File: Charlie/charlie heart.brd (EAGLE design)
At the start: 46.7 x 57.7 mm, 32 parts, among them Q1 BSS84, U1 ATTINY841

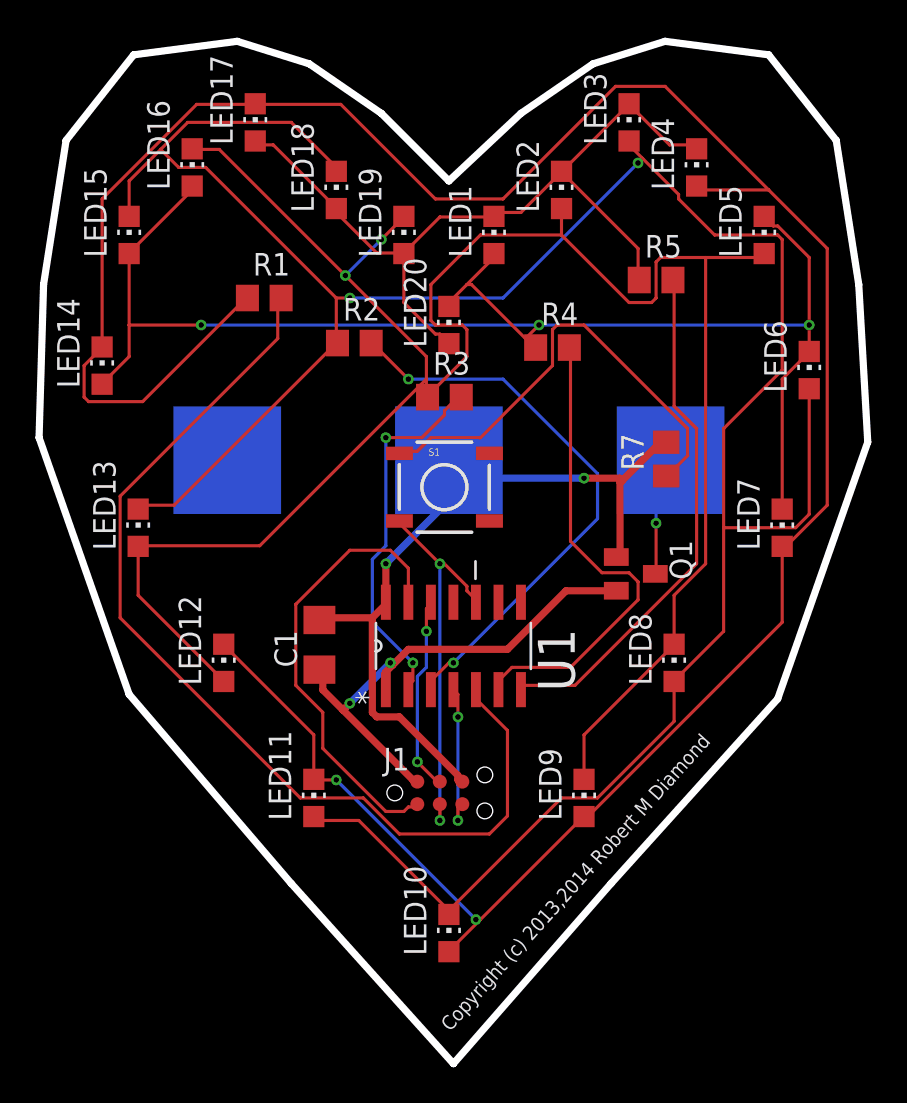
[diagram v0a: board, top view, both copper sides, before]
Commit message: add jumpers for serial and beat sensor
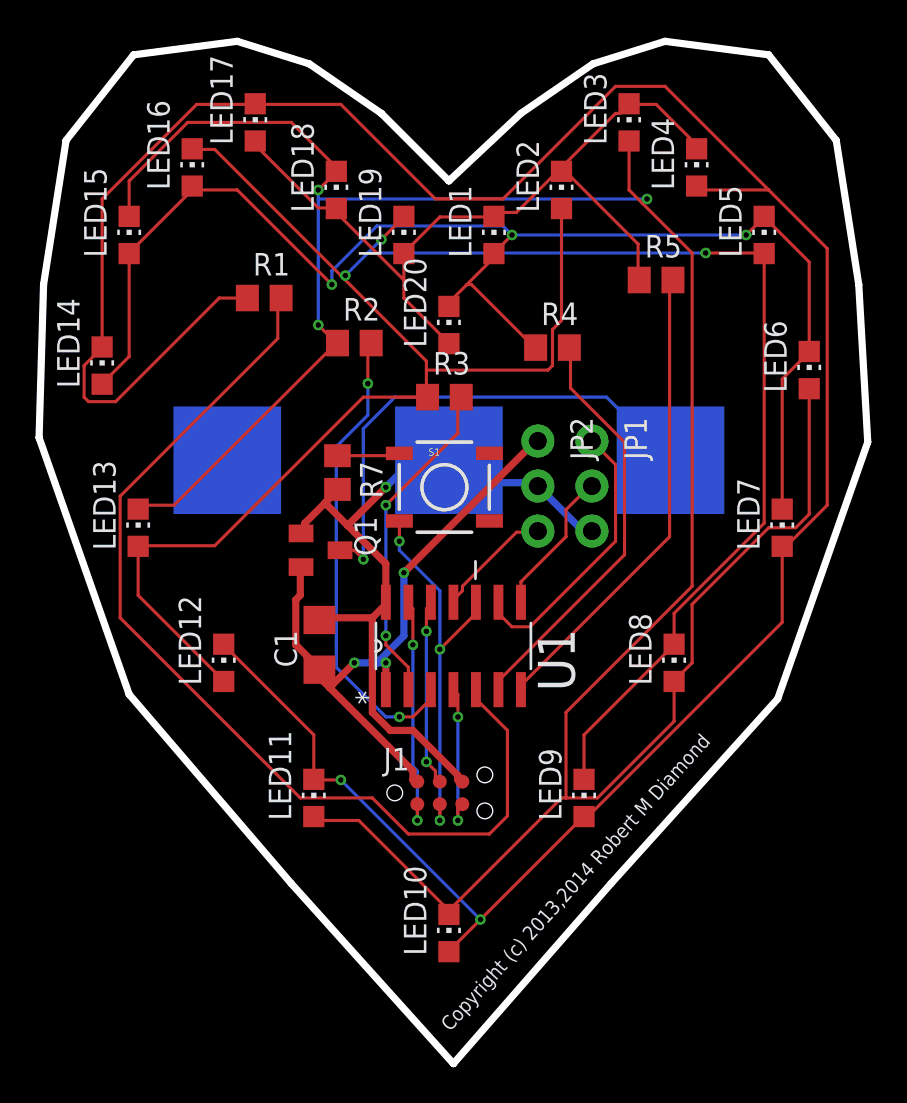
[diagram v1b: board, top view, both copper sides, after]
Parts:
- added JP1, JP2: (no value), SparkFun:1X03_NO_SILK
- moved R7 18.6 mm to (17.8, 34.9), turned to 270 degrees
- moved Q1 17.8 mm to (16.9, 30.5)
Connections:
- net 2.8V: now also JP2.1
- net BEAT_SENSOR: now also JP2.3
- net GND: now also JP1.3, JP2.2
- net RXD1: now also JP1.1
- net TXD1: now also JP1.2
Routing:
- net N$3: track 26.1 -> 3.62 mm
- net N$2: track 6.80 -> 28.4 mm
- net RXD1: track 0.00 -> 15.7 mm
- net MISO: track 25.7 -> 13.4 mm, vias 0 -> 2
- net TXD1: track 0.00 -> 8.27 mm
- net 2.8V: track 28.5 -> 36.7 mm, vias 2 -> 3
- net BEAT_SENSOR: track 0.00 -> 6.64 mm
- net LEDCONTROL2: track 121.8 -> 127.2 mm, vias 2 -> 3
- net L3: track 32.0 -> 26.6 mm
- net LEDCONTROL3: track 148.7 -> 152.8 mm, vias 2 -> 3
- net L1: track 27.0 -> 23.6 mm
- net L0: track 29.6 -> 26.8 mm
- net L2: track 20.9 -> 18.9 mm
- net LEDCONTROL1: track 81.2 -> 79.5 mm
- net GND: track 45.2 -> 43.9 mm, vias 2 -> 1
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
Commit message: update program lines
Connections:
- removed net BUTTON/SCK: J1.3, S1.3, U1.10
- removed net L2: R3.2, U1.2
- removed net RXD1: JP1.1, U1.9
- removed net TXD1: JP1.2, U1.8
- new net BUTTON: S1.3, U1.10
- new net RXD0: JP1.1, U1.5
- new net SCK/L2: J1.3, R3.2, U1.9
- new net TXD0: JP1.2, U1.6
- net L0: now also U1.13; no longer U1.7
- net L1: now also U1.12; no longer U1.6
- net L3: now also U1.2; no longer U1.3
- net L4: now also U1.3; no longer U1.5
- net MISO: now also U1.8; no longer U1.13
- net MOSI: now also U1.7; no longer U1.12
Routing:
- net SCK/L2: track 0.00 -> 52.9 mm
- net RXD0: track 0.00 -> 32.7 mm, vias 0 -> 1
- net L4: track 57.1 -> 26.8 mm, vias 0 -> 2
- net BUTTON/SCK: track 22.3 -> 0.00 mm, vias 3 -> 0
- net L2: track 18.9 -> 0.00 mm, vias 2 -> 0
- net RXD1: track 15.7 -> 0.00 mm
- net TXD0: track 0.00 -> 14.8 mm
- net LEDCONTROL4: track 151.3 -> 139.8 mm, vias 2 -> 0
- net LEDCONTROL2: track 127.2 -> 117.3 mm, vias 3 -> 2
- net TXD1: track 8.27 -> 0.00 mm
- net L1: track 23.6 -> 31.8 mm
- net BUTTON: track 0.00 -> 7.12 mm, vias 0 -> 2
- net L3: track 26.6 -> 21.5 mm
- net 2.8V: track 36.7 -> 41.5 mm, vias 3 -> 2
- net LEDCONTROL3: track 152.8 -> 157.6 mm, vias 3 -> 0
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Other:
- board text added: "GND"
- board text added: "RXD"
- board text added: "Sensor"
- board text added: "TXD"
- board text added: "Vcc"
